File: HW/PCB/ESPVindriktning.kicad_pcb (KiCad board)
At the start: 2 copper layers, 38 x 75 mm, 111 parts, among them P101 TestPoint_Small, P102 TestPoint_Small, P103 TestPoint_Small, P104 TestPoint_Small, P105 TestPoint_Small, P106 TestPoint_Small, P107 TestPoint_Small, P108 TestPoint_Small, P109 TestPoint_Small, P110 TestPoint_Small, P111 TestPoint_Small, P112 TestPoint_Small, P113 TestPoint_Small, P114 TestPoint_Small, P115 TestPoint_Small, P116 TestPoint_Small, P117 TestPoint_Small, P118 TestPoint_Small, P119 TestPoint_Small, P120 TestPoint_Small, P121 TestPoint_Small, P122 TestPoint_Small, P123 TestPoint_Small, P124 TestPoint_Small, P125 TestPoint_Small, P126 TestPoint_Small, P127 TestPoint_Small, P128 TestPoint_Small, P129 TestPoint_Small, P130 TestPoint_Small, P131 TestPoint_Small, P132 TestPoint_Small, P134 TestPoint_Small, P135 TestPoint_Small, P136 TestPoint_Small, P137 TestPoint_Small, SW101 reset, SW102 boot, T101 BSS138, T102 BSS138, X101 USB_C, X102 WS2812, X105 Fan, X106 PM1006, X107 I2C

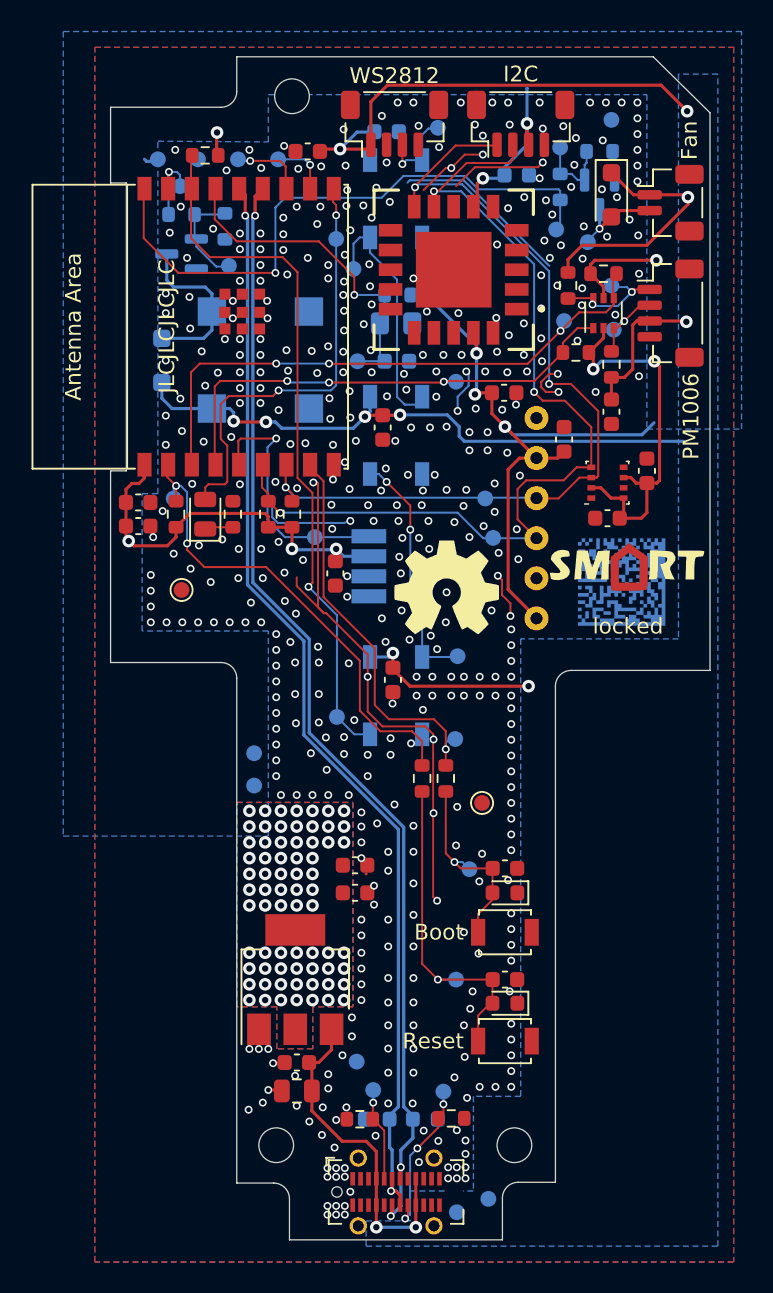
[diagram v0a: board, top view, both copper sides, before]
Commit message: Add panelization configuration and prepare for sample production
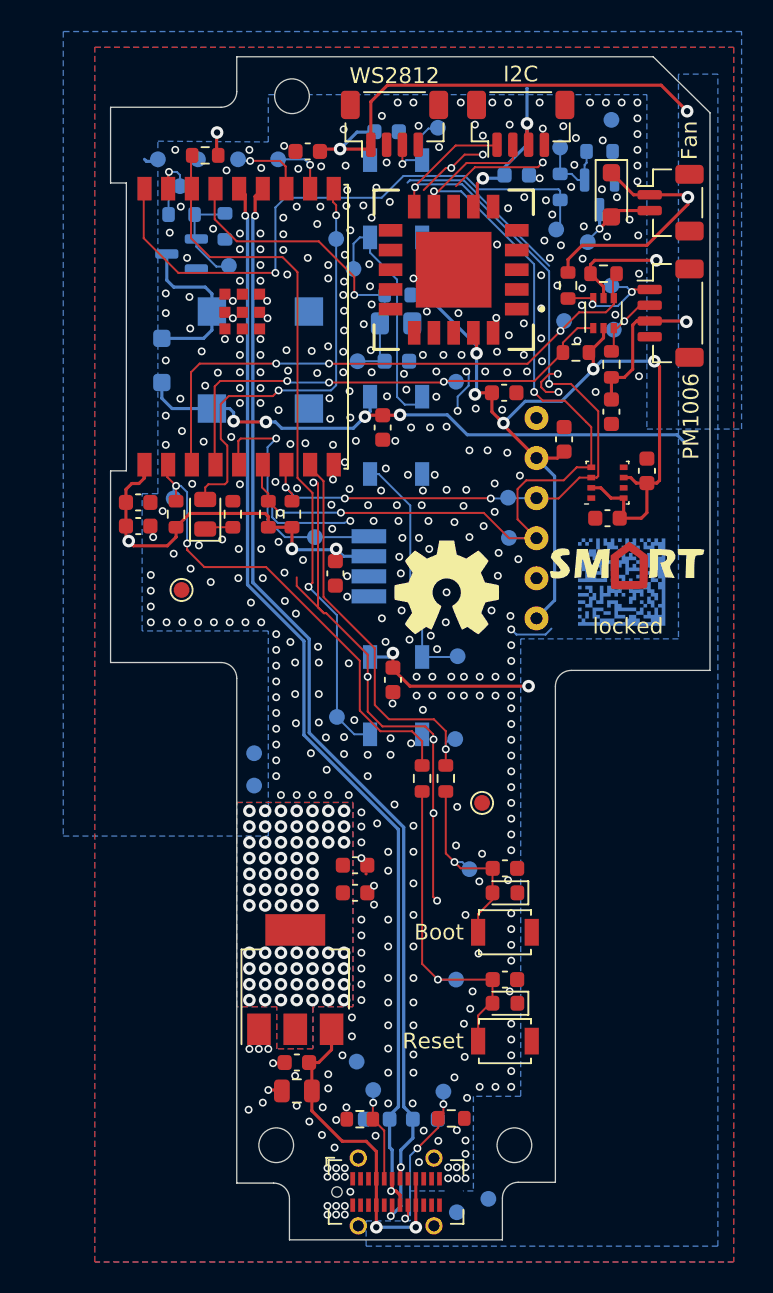
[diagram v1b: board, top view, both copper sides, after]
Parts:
- added REF**: Tab, PCM_kikit:Tab, F.Cu at (109.8, 49.8)
- added REF**: Tab, PCM_kikit:Tab, F.Cu at (91.8, 55.5)
- added REF**: Tab, PCM_kikit:Tab, F.Cu at (109.8, 125.2)
- added REF**: Tab, PCM_kikit:Tab, F.Cu at (91.8, 85.2)
- added REF**: Tab, PCM_kikit:Tab, F.Cu at (130.2, 55.5)
- added REF**: Tab, PCM_kikit:Tab, F.Cu at (130.2, 85.2)
- moved P125 1.45 mm to (117.2, 78.0)
- moved P124 1.00 mm to (117.2, 80.5)
- moved G*** 0.10 mm to (124.8, 82.2) (x2)
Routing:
- net +3.3V: track 112.7 -> 108.8 mm
- net /I2C_SCL: track 60.5 -> 62.3 mm, vias 3 -> 4
- net /I2C_SDA: track 56.8 -> 56.9 mm, vias 3 -> 5
- net GND: vias 441 -> 437
- net /WS2812_1_DO: vias 2 -> 0
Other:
- board text removed: "JLCJLCJLCJLC"

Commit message: Even more PCB layout cleanup
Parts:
- moved P108 2.26 mm to (118.7, 59.3)
- moved P125 0.70 mm to (116.5, 78.0)
- moved P113 0.67 mm to (96.0, 84.2)
- moved P124 0.51 mm to (117.3, 81.0)
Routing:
- net GND: track 73.3 -> 79.1 mm, vias 437 -> 517
- net /FAN: track 38.5 -> 36.4 mm
- net /I2C_SDA: track 56.9 -> 57.6 mm
- net /~{RESET}: track 31.3 -> 31.9 mm
- net /TX: track 7.58 -> 7.07 mm
- net /IR_OUT: track 16.1 -> 16.6 mm
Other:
- board text added: "Status"

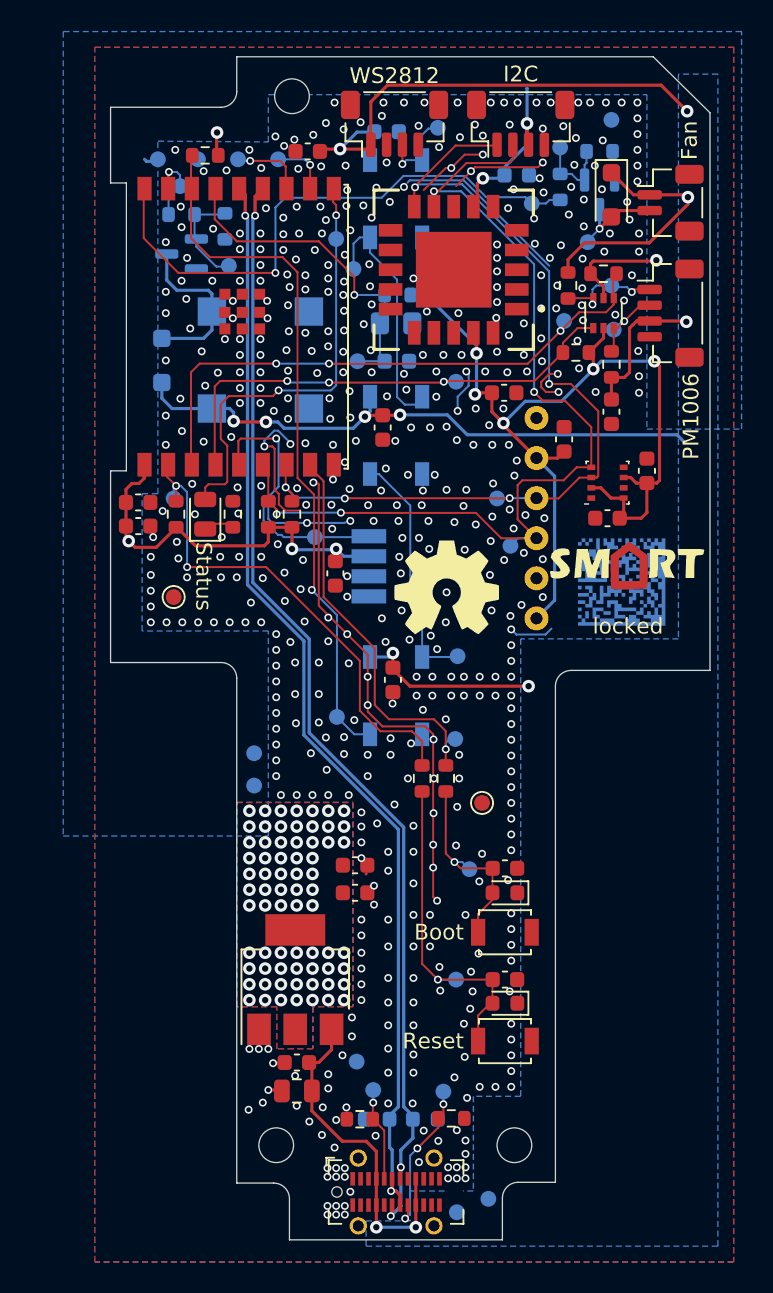
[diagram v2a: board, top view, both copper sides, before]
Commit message: Change Copper Pour distance to 0.3mm
Rework GND plane stitching and copper fillings.
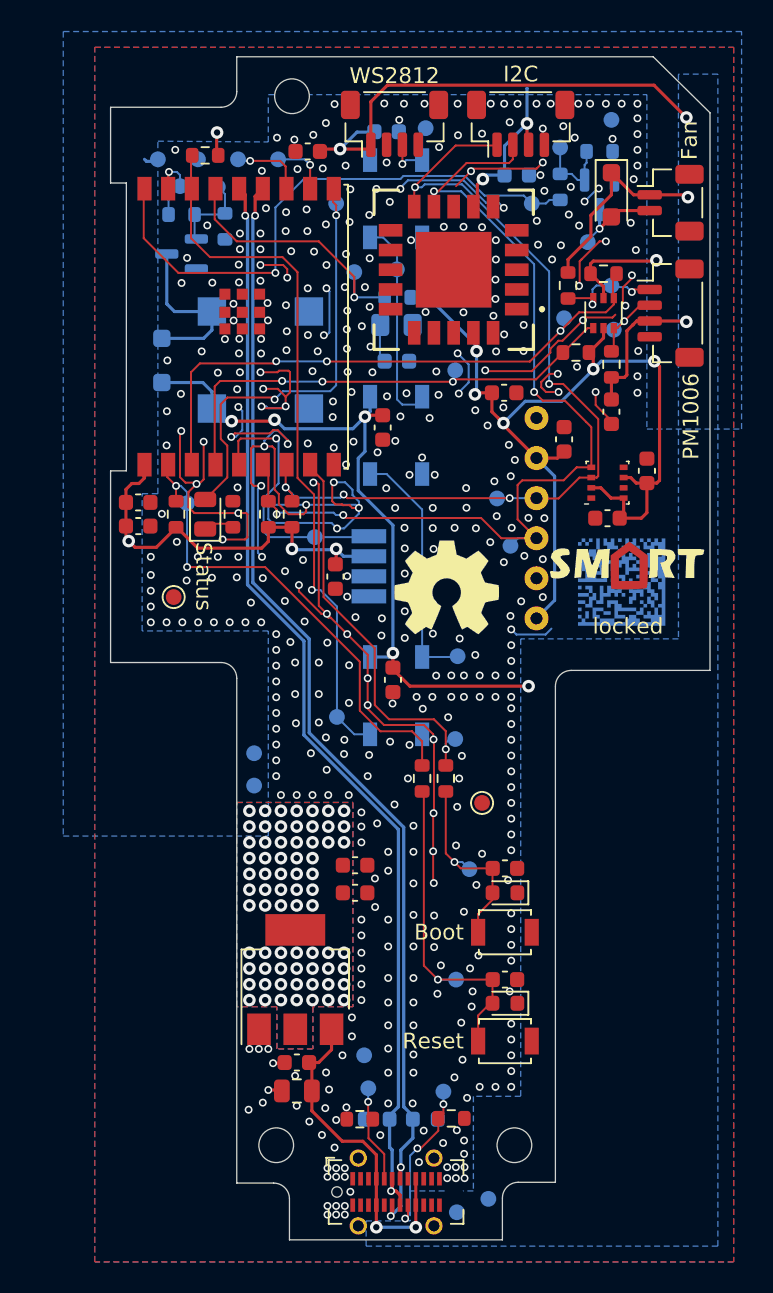
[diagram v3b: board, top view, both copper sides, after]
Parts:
- removed the REF** at (113.3, 83.7)
- moved P121 5.65 mm to (107.5, 63.6)
- moved P132 5.05 mm to (98.8, 58.2)
- moved P107 2.75 mm to (110.2, 63.5)
- moved P127 2.25 mm to (106.3, 59.3)
- moved P106 0.90 mm to (96.8, 78.3)
- moved P112 0.78 mm to (112.0, 54.5)
- moved P122 0.73 mm to (113.8, 69.9)
- moved P111 0.62 mm to (108.1, 113.3)
- moved P104 0.33 mm to (108.3, 115.4)
- moved C113 0.20 mm to (106.2, 83.0)
- moved P117 0.17 mm to (120.8, 66.6)
- moved R104 0.15 mm to (110.2, 65.2)
- moved PD101 0.10 mm to (110.1, 67.0)
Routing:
- net GND: track 79.1 -> 151.6 mm, vias 517 -> 443
- net +5V: track 128.6 -> 121.3 mm, vias 12 -> 11
- net /WS2812_2_DO: track 15.4 -> 13.4 mm
- net /BUZ_G: track 6.67 -> 5.61 mm
- net /~{RESET}: track 31.9 -> 31.0 mm
- net /WS2812_3_DO: track 5.39 -> 4.65 mm

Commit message: Cleanup of the Silkscreen layer and minor changes in routing
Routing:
- net +3.3V: track 108.7 -> 107.8 mm
- net GND: track 151.6 -> 151.7 mm, vias 443 -> 444
